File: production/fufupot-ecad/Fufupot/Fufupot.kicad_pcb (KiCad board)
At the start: 2 copper layers, 6 parts, among them U2 ATMEGA328P-PN

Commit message: Updates unfinished
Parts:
- removed 16MHz1: Crystal, 16 MHz Xtal Osc:XTAL_ABL-16_ABR
- removed C1: 22pF, 22 pF Cap:CAP_K-SERIES_15-L2_VIS
- removed the C2 at (86.4, 86.4)
- removed C3: 10uF, 10 uF Cap:CAP_YX_5X11_RUB
- removed R1: 10k, 10K Ohm:CAP_YX_5X11_RUB
- removed the U2 at (96.2, 66.4)
- added C2: 100n, Capacitor_SMD:C_0805_2012Metric, F.Cu at (142.6, 126.6)
- added C2: 100n, Capacitor_SMD:C_0805_2012Metric, F.Cu at (164.2, 88.9)
- added F1: 500mA, Fuse:Fuse_1210_3225Metric, F.Cu at (130.9, 107.6)
- added F1: 500mA, Fuse:Fuse_1210_3225Metric, F.Cu at (126.0, 143.1)
- added J2: USB_B, Connector_USB:USB_Micro-B_Amphenol_10104110_Horizontal, F.Cu at (129.1, 123.9)
- added J2: USB_B, Connector_USB:USB_Micro-B_Amphenol_10104110_Horizontal, F.Cu at (135.9, 85.4)
- added R10: 1k, Resistor_SMD:R_0805_2012Metric, F.Cu at (164.2, 109.2)
- added R10: 1k, Resistor_SMD:R_0805_2012Metric, F.Cu at (146.4, 139.3)
- added R11: 1k, Resistor_SMD:R_0805_2012Metric, F.Cu at (159.1, 111.8)
- added R11: 1k, Resistor_SMD:R_0805_2012Metric, F.Cu at (146.4, 142.2)
- added R4: 10k, Resistor_SMD:R_0805_2012Metric, F.Cu at (164.2, 94.0)
- added R4: 10k, Resistor_SMD:R_0805_2012Metric, F.Cu at (146.4, 130.4)
- added R8: 1k, Resistor_SMD:R_0805_2012Metric, F.Cu at (164.2, 99.1)
- added R8: 1k, Resistor_SMD:R_0805_2012Metric, F.Cu at (146.4, 133.4)
- added R9: 1k, Resistor_SMD:R_0805_2012Metric, F.Cu at (164.2, 104.1)
- added R9: 1k, Resistor_SMD:R_0805_2012Metric, F.Cu at (146.4, 136.3)
- added SW2: SW_Push, Button_Switch_SMD:SW_DIP_SPSTx04_Slide_6.7x11.72mm_W6.73mm_P2.54mm_LowProfile_JPin, F.Cu at (139.0, 135.7)
- added SW2: SW_Push, Button_Switch_SMD:SW_DIP_SPSTx04_Slide_6.7x11.72mm_W6.73mm_P2.54mm_LowProfile_JPin, F.Cu at (146.6, 102.9)
- added U1: USBLC6-2SC6, Package_TO_SOT_SMD:SOT-23-6, F.Cu at (143.0, 122.8)
- added U1: USBLC6-2SC6, Package_TO_SOT_SMD:SOT-23-6, F.Cu at (153.8, 84.8)
- added U2: LM5165DRC, Package_SON:Texas_S-PVSON-N10_ThermalVias, F.Cu at (145.3, 84.8)
- added U2: LM5165DRC, Package_SON:Texas_S-PVSON-N10_ThermalVias, F.Cu at (137.7, 123.3)
- added U3: FT232RL, Package_SO:SSOP-28_5.3x10.2mm_P0.65mm, F.Cu at (128.5, 135.0)
- added U3: FT232RL, Package_SO:SSOP-28_5.3x10.2mm_P0.65mm, F.Cu at (125.9, 97.4)
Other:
- board outline added: 127 x 127 mm
- copper layers 2 -> 4

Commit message: pcb update
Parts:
- removed the C2 at (142.6, 126.6)
- removed the C2 at (164.2, 88.9)
- removed the F1 at (130.9, 107.6)
- removed the F1 at (126.0, 143.1)
- removed the J2 at (129.1, 123.9)
- removed the J2 at (135.9, 85.4)
- removed the R10 at (164.2, 109.2)
- removed the R10 at (146.4, 139.3)
- removed the R11 at (159.1, 111.8)
- removed the R11 at (146.4, 142.2)
- removed the R4 at (164.2, 94.0)
- removed the R4 at (146.4, 130.4)
- removed the R8 at (164.2, 99.1)
- removed the R8 at (146.4, 133.4)
- removed the R9 at (164.2, 104.1)
- removed the R9 at (146.4, 136.3)
- removed the SW2 at (139.0, 135.7)
- removed the SW2 at (146.6, 102.9)
- removed the U1 at (143.0, 122.8)
- removed the U1 at (153.8, 84.8)
- removed the U2 at (145.3, 84.8)
- removed the U2 at (137.7, 123.3)
- removed the U3 at (128.5, 135.0)
- removed the U3 at (125.9, 97.4)
- added C2: 100n, Capacitor_SMD:C_0805_2012Metric, F.Cu at (109.6, 93.5)
- added F1: 500mA, Fuse:Fuse_1210_3225Metric, F.Cu at (93.0, 110.1)
- added J2: USB_B, Connector_USB:USB_Micro-B_Amphenol_10104110_Horizontal, F.Cu at (96.1, 90.9)
- added R10: 1k, Resistor_SMD:R_0805_2012Metric, F.Cu at (113.4, 106.3)
- added R11: 1k, Resistor_SMD:R_0805_2012Metric, F.Cu at (113.4, 109.2)
- added R4: 10k, Resistor_SMD:R_0805_2012Metric, F.Cu at (113.4, 97.4)
- added R8: 1k, Resistor_SMD:R_0805_2012Metric, F.Cu at (113.4, 100.4)
- added R9: 1k, Resistor_SMD:R_0805_2012Metric, F.Cu at (113.4, 103.3)
- added SW2: SW_Push, Button_Switch_SMD:SW_DIP_SPSTx04_Slide_6.7x11.72mm_W6.73mm_P2.54mm_LowProfile_JPin, F.Cu at (106.0, 102.7)
- added U1: USBLC6-2SC6, Package_TO_SOT_SMD:SOT-23-6, F.Cu at (110.0, 89.8)
- added U2: LM5165DRC, Package_SON:Texas_S-PVSON-N10_ThermalVias, F.Cu at (104.7, 90.3)
- added U3: FT232RL, Package_SO:SSOP-28_5.3x10.2mm_P0.65mm, F.Cu at (95.5, 102.0)
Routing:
- added copper zone on In1.Cu, net GND

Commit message: Kicad updates yay
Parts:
- added C1: 1uF, Capacitor_SMD:C_0805_2012Metric, F.Cu at (113.3, 73.7)
- added C10: 3.3 uF 275V, KiCad:ECQUAAF335LD, F.Cu at (123.5, 99.1)
- added C11: 0.1uF 63V, 8600footprint:CAP_WCAP-ATG5_05.0X11.0_WRE, F.Cu at (135.2, 68.6)
- added C12: 0.37uF 1200V, ECWfootprints:CAP_ECWFL_STRAIGHT_20.5LX11.9TX18.5H_PAN, F.Cu at (112.0, 58.4)
- added C3: 33nF, Capacitor_SMD:C_0805_2012Metric, F.Cu at (116.4, 78.1)
- added C4: 10uF, Capacitor_SMD:C_0805_2012Metric, F.Cu at (116.4, 81.1)
- added C9: 10uF 25V, footprints:U1-E_NCH, F.Cu at (132.6, 83.8)
- added IC1: FOD3150, FODfootprints:SMD8_9P91X6P86_ONS, F.Cu at (125.0, 118.1)
- added J1: Conn_01x04, 4PINfootprints:CONN_B4B-XH-A_JST, F.Cu at (86.5, 142.5)
- added J10: Conn_01x03, 3PINfootprints:CONN_B3B-ZR_JST, F.Cu at (72.7, 122.5)
- added J11: Conn_01x03, 3PINfootprints:CONN_B3B-ZR_JST, F.Cu at (72.7, 127.7)
- added J12: Conn_01x02, B2B-XH-A_LF__SN_:JST_B2B-XH-A_LF__SN_, F.Cu at (62.2, 154.4)
- added J3: Conn_01x03, 3PINfootprints:CONN_B3B-ZR_JST, F.Cu at (72.7, 117.3)
- added J4: Conn_01x02, B2B-XH-A_LF__SN_:JST_B2B-XH-A_LF__SN_, F.Cu at (62.2, 117.9)
- added J5: Conn_01x02, B2B-XH-A_LF__SN_:JST_B2B-XH-A_LF__SN_, F.Cu at (62.2, 125.2)
- added J6: Conn_01x02, B2B-XH-A_LF__SN_:JST_B2B-XH-A_LF__SN_, F.Cu at (62.2, 132.5)
- added J7: Conn_01x02, B2B-XH-A_LF__SN_:JST_B2B-XH-A_LF__SN_, F.Cu at (62.2, 139.8)
- added J8: Conn_01x04, 4PINfootprints:CONN_B4B-XH-A_JST, F.Cu at (86.5, 149.9)
- added J9: Conn_01x02, B2B-XH-A_LF__SN_:JST_B2B-XH-A_LF__SN_, F.Cu at (62.2, 147.1)
- added L1: 47uH, Inductor_SMD:L_0805_2012Metric, F.Cu at (120.9, 83.8)
- added L3: 10uH, INDPM:INDPM176169X700N, F.Cu at (93.8, 66.0)
- added R1: 200, Resistor_SMD:R_0805_2012Metric, F.Cu at (103.2, 118.2)
- added R12: 10k, Resistor_SMD:R_0805_2012Metric, F.Cu at (69.6, 134.2)
- added R13: 10k, Resistor_SMD:R_0805_2012Metric, F.Cu at (69.6, 137.2)
- added R14: 330, Resistor_SMD:R_0805_2012Metric, F.Cu at (151.5, 115.6)
- added R15: 16, Resistor_SMD:R_0805_2012Metric, F.Cu at (151.5, 118.6)
- added R16: 10k, Resistor_SMD:R_0805_2012Metric, F.Cu at (151.5, 121.5)
- added R17: 0.1 5W, SQPfootprints:RES_SQP500_22X9P5_YAG, F.Cu at (126.5, 137.2)
- added R18: 3.3k, Resistor_SMD:R_0805_2012Metric, F.Cu at (151.5, 124.5)
- added R19: 0, Resistor_SMD:R_0805_2012Metric, F.Cu at (103.2, 124.0)
- added R2: 330, Resistor_SMD:R_0805_2012Metric, F.Cu at (103.2, 121.1)
- added R20: 0, Resistor_SMD:R_0805_2012Metric, F.Cu at (103.2, 127.0)
- added R3: 100kOhm, Resistor_SMD:R_0805_2012Metric, F.Cu at (120.8, 75.1)
- added R5: 820kOhm, Resistor_SMD:R_0805_2012Metric, F.Cu at (120.8, 78.0)
- added R6: 68kOhm, Resistor_SMD:R_0805_2012Metric, F.Cu at (120.8, 81.0)
- added R7: 1k, Resistor_SMD:R_0805_2012Metric, F.Cu at (69.6, 131.3)
- added U5: STGP8NC60KD, TO225P1040X460X1968-3(1):TO225P1040X460X1968-3, F.Cu at (68.6, 83.2)
- moved U1 29.1 mm to (82.4, 80.3)
- moved U2 25.2 mm to (79.5, 90.3)
- moved U3 15.8 mm to (79.8, 104.4)
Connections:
- U3 pad 18: GND -> unconnected-(U3-GND-Pad18)
- U3 pad 21: GND -> unconnected-(U3-GND-Pad21)
- U3 pad 7: GND -> unconnected-(U3-GND-Pad7)

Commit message: Fixed switches
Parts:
- added 16MHz1: Crystal, crystalfootprints:XTAL_ABL-16_ABR, F.Cu at (108.5, 137.6)
- added C5: 22pF, 22pFfootprints:CAP_K-SERIES_15-L2_VIS, F.Cu at (115.8, 142.5)
- added C6: 22pF, 22pFfootprints:CAP_K-SERIES_15-L2_VIS, F.Cu at (115.8, 146.8)
- added C7: 10uF, 10uFfootprints:CAP_YX_5X11_RUB, F.Cu at (117.4, 152.4)
- added C8: 0.1 uF, 0.1uFfootprints:CAP_Y5VE5TL2_VIS, F.Cu at (120.3, 137.0)
- added SW1: SW_Push, TS02-66-50-BK-100-SCR-D:SW_TS02-66-50-BK-100-SCR-D, F.Cu at (108.3, 147.1)
- added U4: ATMEGA328P-PN, ATmegafootprints:28P3_ATM, F.Cu at (60.3, 43.2)
- SW2: footprint Button_Switch_SMD:SW_DIP_SPSTx04_Slide_6.7x11.72mm_W6.73mm_P2.54mm_LowProfile_JPin -> TS02-66-50-BK-100-SCR-D:SW_TS02-66-50-BK-100-SCR-D

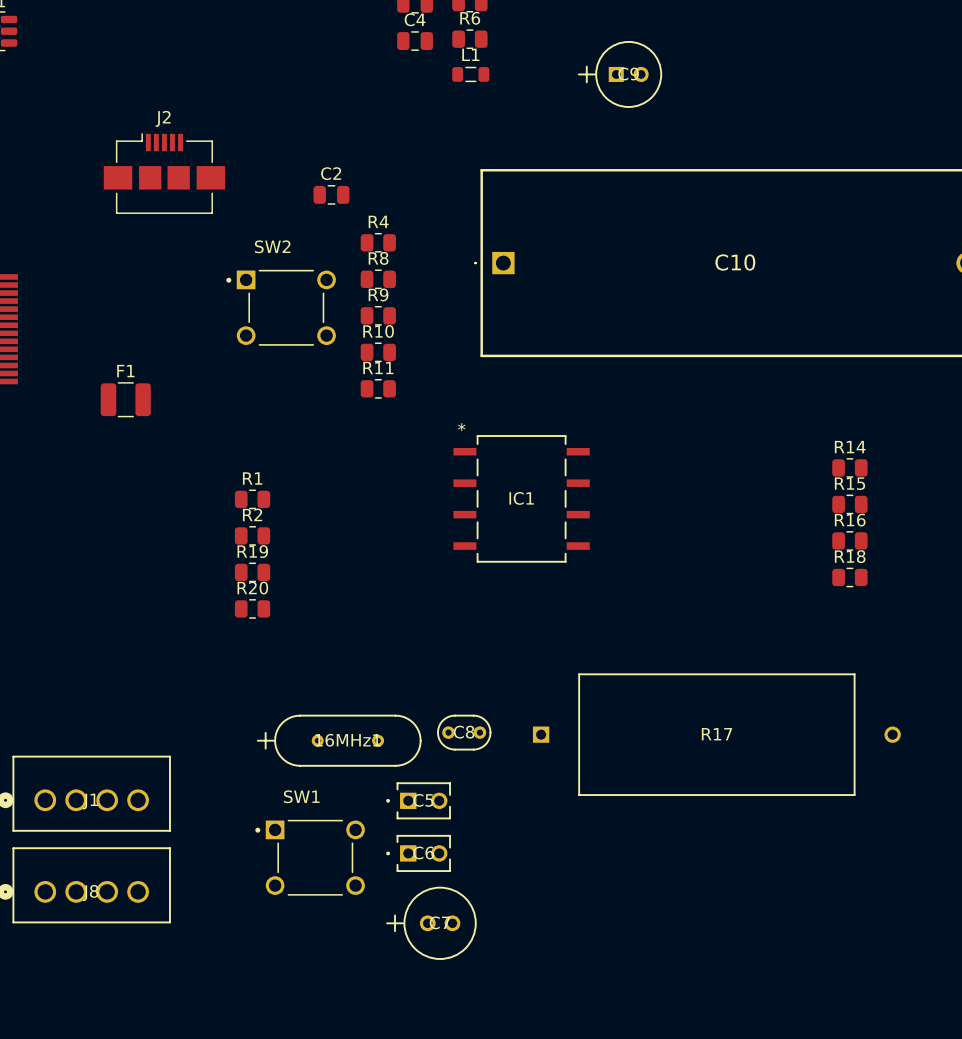
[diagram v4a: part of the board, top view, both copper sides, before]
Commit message: Updating USB
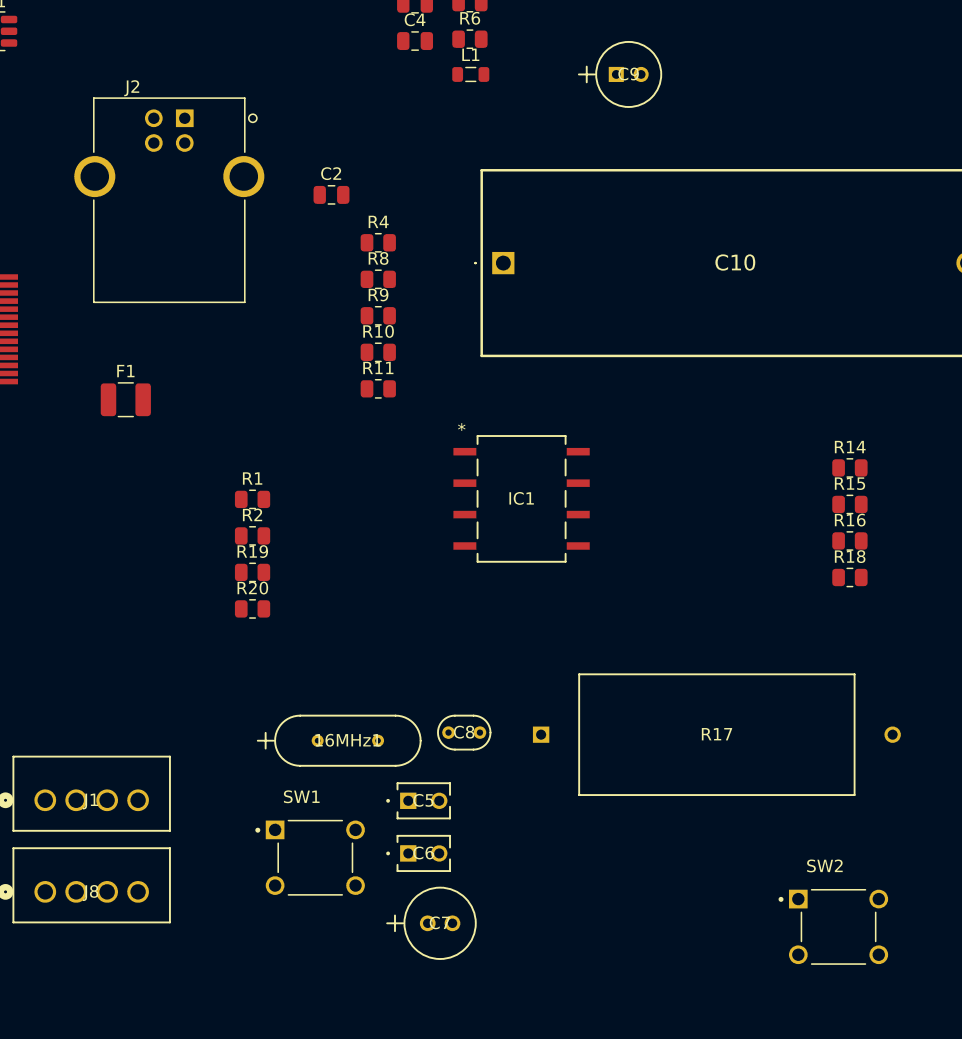
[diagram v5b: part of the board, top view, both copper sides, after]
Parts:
- J2: footprint Connector_USB:USB_Micro-B_Amphenol_10104110_Horizontal -> UJ2-BH-W1-TH:CUI_UJ2-BH-W1-TH
- moved SW2 67.0 mm to (150.6, 152.7)
- moved J2 3.88 mm to (97.8, 87.4)

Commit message: Update Fufupot.kicad_pcb
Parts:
- moved J2 50.2 mm to (73.3, 43.5)
- moved U3 32.5 mm to (54.4, 84.2)
- moved U2 25.7 mm to (64.3, 69.6)
- moved U5 20.3 mm to (68.6, 62.9)
- moved U1 11.1 mm to (75.1, 72.1)
- moved U4 9.86 mm to (50.8, 40.6)
- moved C10 2.54 mm to (123.5, 96.5)
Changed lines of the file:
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@@
   )
   (footprint "TO225P1040X460X1968-3(1):TO225P1040X460X1968-3" (layer "F.Cu")
-    (at 68.57 83.215)
+    (at 68.57 62.895)
     (property "Sheetfile" "Fufupot.kicad_sch")
     (property "Sheetname" "")
@@
   )
   (footprint "Package_TO_SOT_SMD:SOT-23-6" (layer "F.Cu")
-    (at 82.4175 80.33)
+    (at 75.0625 72.07)
     (descr "SOT, 6 Pin (https://www.jedec.org/sites/default/files/docs/Mo-178c.PDF variant AB), generated with kicad-footprint-generator ipc_gullwing_generator.py")
     (tags "SOT TO_SOT_SMD")
@@
         (effects (font (size 1 1) (thickness 0.15)))
     )
-    (fp_text value "0.37uF 1200V" (at 8.75 0 unlocked) (layer "F.Fab")
+    (fp_text value "0.37uF 1200V" (at 8.75 -7.62 unlocked) (layer "F.Fab")
         (effects (font (size 1 1) (thickness 0.15)))
     )
@@
   )
   (footprint "KiCad:ECQUAAF335LD" (layer "F.Cu")
-    (at 123.49 99.06)
+    (at 123.49 96.52)
     (descr "ECQUAAF335LD-2")
     (tags "Capacitor")
@@
         (effects (font (size 1 1) (thickness 0.15)))
     )
-    (fp_text value "0.1uF 63V" (at 1 0 unlocked) (layer "F.Fab")
+    (fp_text value "0.1uF 63V" (at 4.54 -5.08 unlocked) (layer "F.Fab")
         (effects (font (size 1 1) (thickness 0.15)))
     )
@@
         (effects (font (size 1 1) (thickness 0.15)))
     )
-    (fp_text value "10uF 25V" (at 1.0033 0 unlocked) (layer "F.Fab")
+    (fp_text value "10uF 25V" (at 1.0033 -5.08 unlocked) (layer "F.Fab")
         (effects (font (size 1 1) (thickness 0.15)))
     )
@@
   )
   (footprint "Package_SON:Texas_S-PVSON-N10_ThermalVias" (layer "F.Cu")
-    (at 79.52 90.27)
+    (at 64.28 69.58)
     (descr "3x3mm Body, 0.5mm Pitch, S-PVSON-N10, DRC, http://www.ti.com/lit/ds/symlink/tps61201.pdf")
     (tags "0.5 S-PVSON-N10 DRC")
@@
   )
   (footprint "Package_SO:SSOP-28_5.3x10.2mm_P0.65mm" (layer "F.Cu")
-    (at 79.8 104.405)
+    (at 54.4 84.205)
     (descr "28-Lead Plastic Shrink Small Outline (SS)-5.30 mm Body [SSOP] (see Microchip Packaging Specification 00000049BS.pdf)")
     (tags "SSOP 0.65")
@@
   )
   (footprint "ATmegafootprints:28P3_ATM" (layer "F.Cu")
-    (at 60.325 43.18)
+    (at 50.8 40.64)
     (tags "ATMEGA328P-PN ")
     (property "Sheetfile" "Fufupot.kicad_sch")
@@
   )
   (footprint "UJ2-BH-W1-TH:CUI_UJ2-BH-W1-TH" (layer "F.Cu")
-    (at 97.75075 87.36)
+    (at 73.31 43.55)
     (property "Sheetfile" "Fufupot.kicad_sch")
     (property "Sheetname" "")

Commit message: pcb layout
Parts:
- moved J2 104.2 mm to (132.1, 129.6), turned to 90 degrees
- moved U1 77.2 mm to (125.6, 130.5), turned to 180 degrees
- moved U3 76.5 mm to (118.3, 126.1)
- moved U4 75.4 mm to (91.4, 104.1)
- moved R14 72.1 mm to (115.2, 53.3)
- moved R18 62.4 mm to (115.2, 73.7)
- moved C10 61.9 mm to (71.1, 63.5)
- moved R15 58.1 mm to (133.0, 63.5)
- moved R17 57.0 mm to (115.3, 81.3)
- moved R16 56.1 mm to (133.0, 68.6)
- moved IC1 56.0 mm to (121.4, 62.2)
- moved SW1 53.9 mm to (83.8, 99.1)
- moved C12 52.5 mm to (66.0, 83.8)
- moved SW2 49.2 mm to (116.8, 116.8), turned to 180 degrees
- moved L1 48.9 mm to (98.0, 40.6)
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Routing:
- net GND: track 0.00 -> 116.1 mm, vias 0 -> 20
- net D9: track 0.00 -> 79.1 mm, vias 0 -> 2
- net Net-(IC1-VSS): track 0.00 -> 66.3 mm, vias 0 -> 2
- net A1: track 0.00 -> 54.5 mm, vias 0 -> 2
- net Net-(J4-Pin_1): track 0.00 -> 47.9 mm
- net +5V: track 0.00 -> 33.6 mm, vias 0 -> 9
- net +48V: track 0.00 -> 33.5 mm, vias 0 -> 4
- net Net-(J4-Pin_2): track 0.00 -> 32.7 mm
- net +3V3: track 0.00 -> 20.6 mm, vias 0 -> 1
- net Net-(U4-PB7): track 0.00 -> 19.9 mm
- net Net-(U4-PB6): track 0.00 -> 18.9 mm
- net DTR: track 0.00 -> 16.6 mm
- net SCK: track 0.00 -> 12.7 mm
- net MISO: track 0.00 -> 12.7 mm
- net MOSI: track 0.00 -> 12.7 mm
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- added copper zone on In2.Cu, net +16V
- added copper zone on In2.Cu, net +48V
- added copper zone on In2.Cu, net +5V

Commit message: pcb first design
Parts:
- moved J8 2.54 mm to (91.5, 144.8)
- turned J5 to 90 degrees
- turned R12 to -90 degrees
- turned R13 to -90 degrees
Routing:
- net A2: track 0.00 -> 78.9 mm, vias 0 -> 2
- net A3: track 0.00 -> 78.5 mm, vias 0 -> 2
- net D_LEDStrip: track 0.00 -> 66.5 mm, vias 0 -> 2
- net A5: track 0.00 -> 62.4 mm, vias 0 -> 2
- net A4: track 0.00 -> 60.9 mm, vias 0 -> 2
- net D_Buzz: track 0.00 -> 41.3 mm
- net D_LED: track 0.00 -> 37.5 mm
- net RX: track 0.00 -> 36.2 mm, vias 0 -> 2
- net D_Red: track 0.00 -> 30.0 mm
- net TX: track 0.00 -> 23.8 mm
- net GND: track 116.1 -> 138.7 mm, vias 20 -> 22
- net D_Switch: track 0.00 -> 8.67 mm
- net +5V: track 33.6 -> 39.8 mm
